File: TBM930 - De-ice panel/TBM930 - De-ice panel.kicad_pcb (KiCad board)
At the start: 2 copper layers, 190.5 x 101.6 mm, 48 parts, among them J1 SW_AIRFRAME_DE_ICE, J2 SW_ICE_LIGHT, J3 SW_PROP_DE_ICE, J4 SW_WIND_SHIELD, J5 SW_PITOT_L_HTR, J6 SW_PITOT_R_HTR, J7 SW_INERT_SEP, J8 Barrel_Jack, SW1 SW_Push, SW2 Mini toggle - SPDT, SW3 Mini toggle - SPDT, SW4 Mini toggle - SPDT, SW5 Mini toggle - SPDT, SW6 Mini toggle - SPDT, SW7 Mini toggle - SPDT, SW8 Mini toggle - SPDT, U1 ArduinoMEGA2560PROEmbed, U2 TLC5917IN, U3 TLC5917IN

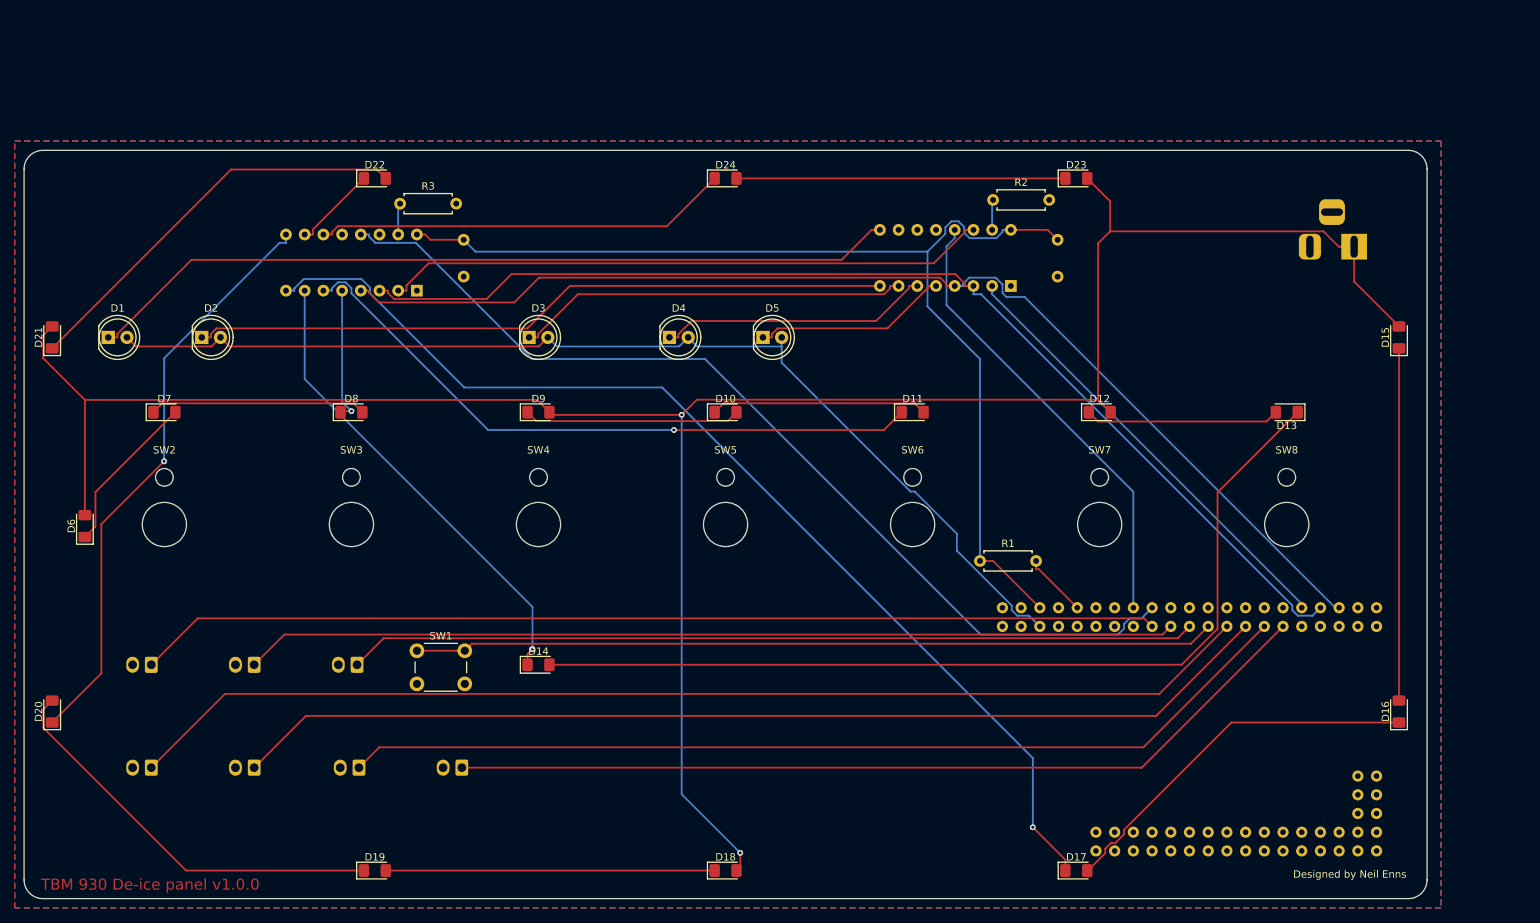
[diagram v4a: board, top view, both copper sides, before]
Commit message: Before switching to Pro Micro
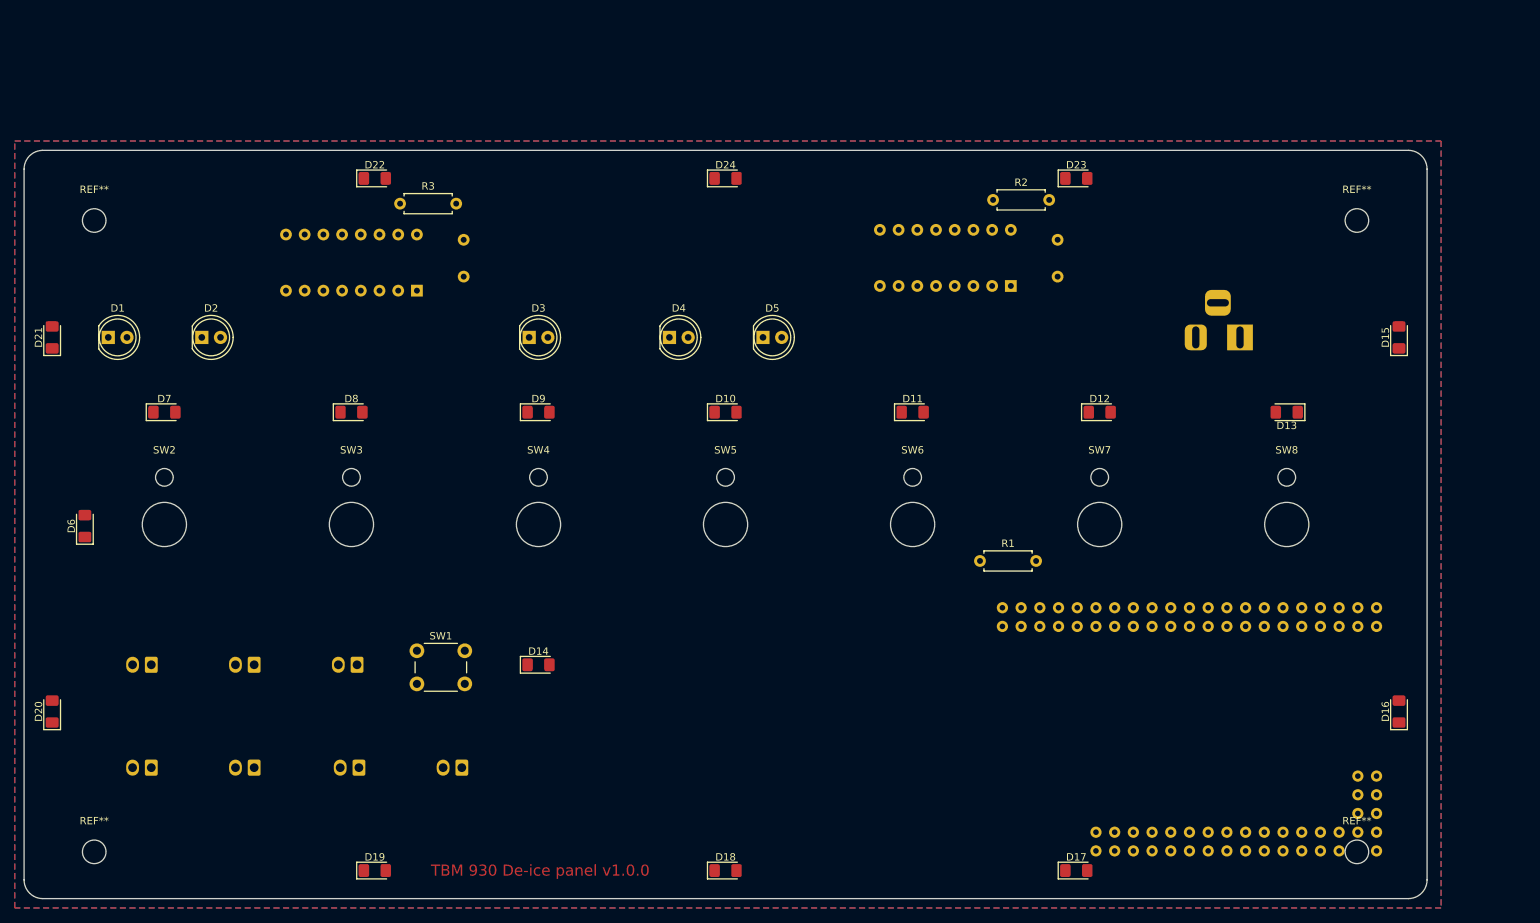
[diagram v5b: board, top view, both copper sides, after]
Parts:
- added REF**: MountingHole_3.2mm_M3, MountingHole:MountingHole_3.2mm_M3, F.Cu at (220.3, 137.8)
- added REF**: MountingHole_3.2mm_M3, MountingHole:MountingHole_3.2mm_M3, F.Cu at (220.3, 52.1)
- added REF**: MountingHole_3.2mm_M3, MountingHole:MountingHole_3.2mm_M3, F.Cu at (48.9, 137.8)
- added REF**: MountingHole_3.2mm_M3, MountingHole:MountingHole_3.2mm_M3, F.Cu at (48.9, 52.1)
- moved J8 19.8 mm to (204.5, 67.9)
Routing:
- net +12V_LED: track 314.9 -> 0.00 mm, vias 2 -> 0
- net LED_LATCH: track 155.6 -> 0.00 mm
- net WIND_SHIELD: track 154.0 -> 0.00 mm
- net LED_CLOCK: track 150.6 -> 0.00 mm
- net +5V: track 148.5 -> 0.00 mm
- net +5V_LED: track 147.5 -> 0.00 mm
- net BACKLIGHT4: track 146.7 -> 0.00 mm, vias 1 -> 0
- net PITOT_L_HTR: track 142.6 -> 0.00 mm
- net AIRFRAME_DE_ICE: track 139.0 -> 0.00 mm
- net BACKLIGHT_BRIGHTNESS: track 132.0 -> 0.00 mm
- net PITOT_R_HTR: track 130.9 -> 0.00 mm
- net Net-(D13-Pad1): track 126.6 -> 0.00 mm
- net ICE_LIGHT: track 126.6 -> 0.00 mm
- net INERT_SEP: track 119.4 -> 0.00 mm
- net PROP_DE_ICE: track 115.2 -> 0.00 mm
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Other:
- board text removed: "Designed by Neil Enns"

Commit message: Switch to smaller Arduino
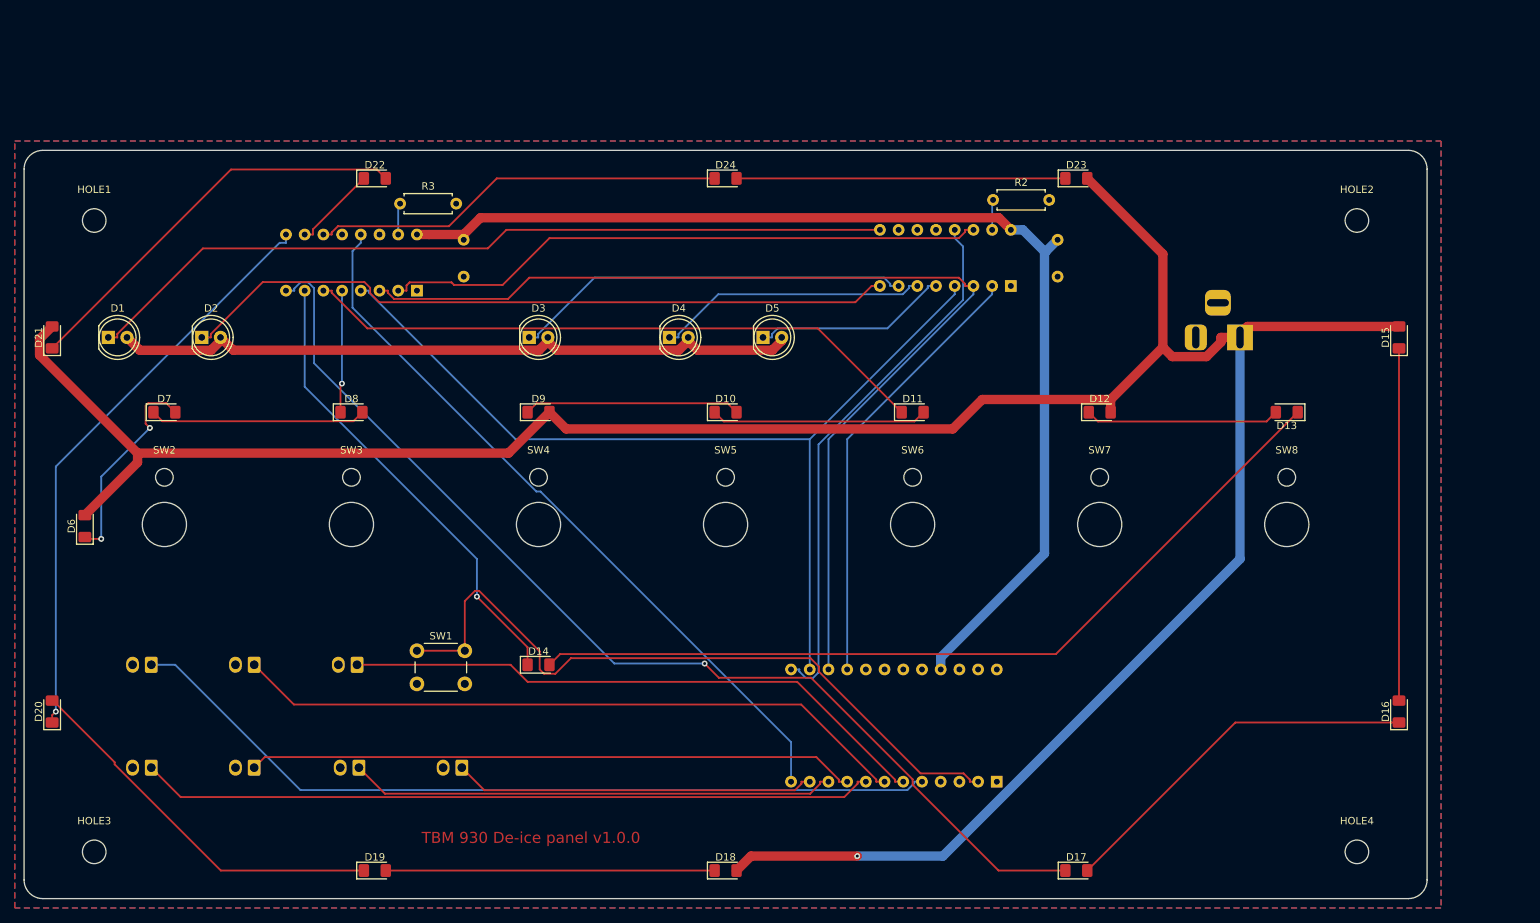
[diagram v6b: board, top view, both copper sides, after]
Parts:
- removed R1: 10k, Resistor_THT:R_Axial_DIN0207_L6.3mm_D2.5mm_P7.62mm_Horizontal
- U1: value ArduinoMEGA2560PROEmbed -> Sparkfun_Pro_Micro; footprint Global MobiFlight panel parts:MEGA2560PROEmbed -> Arduino:Sparkfun_Pro_Micro
- moved U1 54.9 mm to (143.5, 113.0)
- renumbered REF** to HOLE1, REF** to HOLE2, REF** to HOLE3, REF** to HOLE4
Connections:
- U1 pad 10: Net-(U1-Pad10) -> PITOT_R_HTR
- U1 pad 11: Net-(U1-Pad11) -> INERT_SEP
- U1 pad 12: Net-(U1-Pad12) -> BACKLIGHT_BRIGHTNESS
- U1 pad 13: Net-(U1-Pad13) -> ANNUNCIATOR_BRIGHTNESS
- U1 pad 14: Net-(U1-Pad14) -> LED_LATCH
- U1 pad 15: ANNUNCIATOR_BRIGHTNESS -> LED_CLOCK
- U1 pad 16: Net-(U1-Pad16) -> LED_DATA
- U1 pad 17: BACKLIGHT_BRIGHTNESS -> Net-(U1-Pad17)
- U1 pad 18: AIRFRAME_DE_ICE -> Net-(U1-Pad18)
- U1 pad 2: Net-(U1-Pad2) -> LTS_TEST
- U1 pad 20: ICE_LIGHT -> Net-(U1-Pad20)
- U1 pad 21: Net-(U1-Pad21) -> +5V
- U1 pad 22: PROP_DE_ICE -> Net-(U1-Pad22)
- U1 pad 23: Net-(U1-Pad23) -> GND
- U1 pad 24: LTS_TEST -> Net-(U1-Pad24)
- U1 pad 5: +5V -> AIRFRAME_DE_ICE
- U1 pad 6: +5V_LED -> PROP_DE_ICE
- U1 pad 7: Net-(U1-Pad7) -> ICE_LIGHT
- U1 pad 8: Net-(U1-Pad8) -> WIND_SHIELD
- U1 pad 9: Net-(R1-Pad2) -> PITOT_L_HTR
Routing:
- net +12V_LED: track 0.00 -> 361.9 mm, vias 0 -> 1
- net +5V: track 0.00 -> 153.8 mm
- net BACKLIGHT4: track 0.00 -> 145.9 mm, vias 0 -> 1
- net LED_CLOCK: track 0.00 -> 143.3 mm
- net LED_LATCH: track 0.00 -> 129.7 mm
- net Net-(D13-Pad1): track 0.00 -> 115.8 mm
- net AIRFRAME_DE_ICE: track 0.00 -> 112.3 mm
- net AIRFRAME_1: track 0.00 -> 111.1 mm
- net BACKLIGHT_BRIGHTNESS: track 0.00 -> 99.8 mm
- net WIND_SHIELD: track 0.00 -> 99.7 mm
- net LTS_TEST: track 0.00 -> 98.0 mm
- net AIRFRAME_2: track 0.00 -> 97.9 mm
- net +5V_LED: track 0.00 -> 95.2 mm
- net ICE_LIGHT: track 0.00 -> 92.3 mm
- net BACKLIGHT2: track 0.00 -> 85.5 mm
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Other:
- net class +12V_LED added: clearance 0.2, trace_width 1.27, via_dia 0.8, via_drill 0.4
- net class +5V added: clearance 0.2, trace_width 1.27, via_dia 0.8, via_drill 0.4
- net class +5V_LED added: clearance 0.2, trace_width 1.27, via_dia 0.8, via_drill 0.4
- net class GND added: clearance 0.2, trace_width 1.27, via_dia 0.8, via_drill 0.4

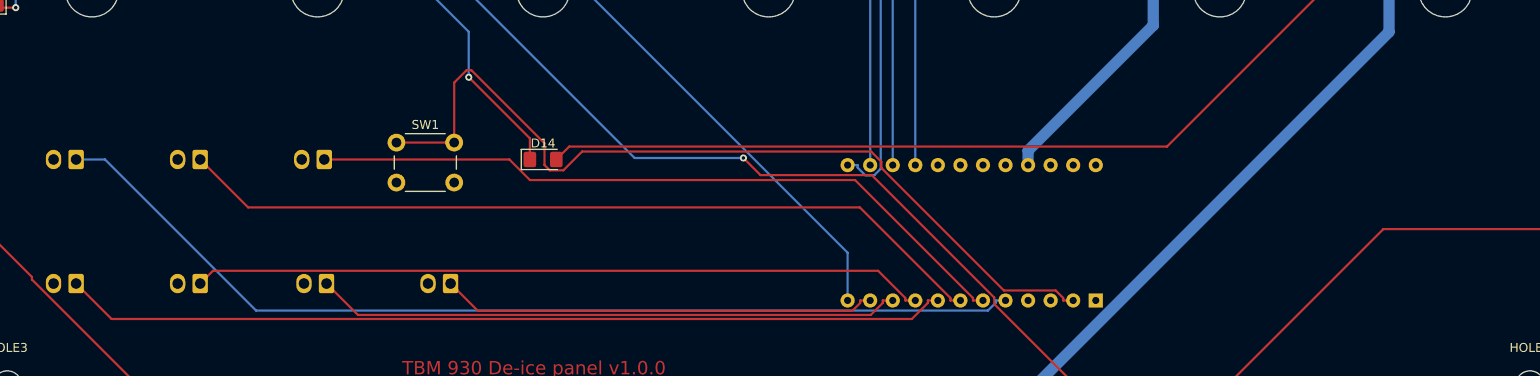
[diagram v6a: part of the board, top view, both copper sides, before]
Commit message: More PCB markings
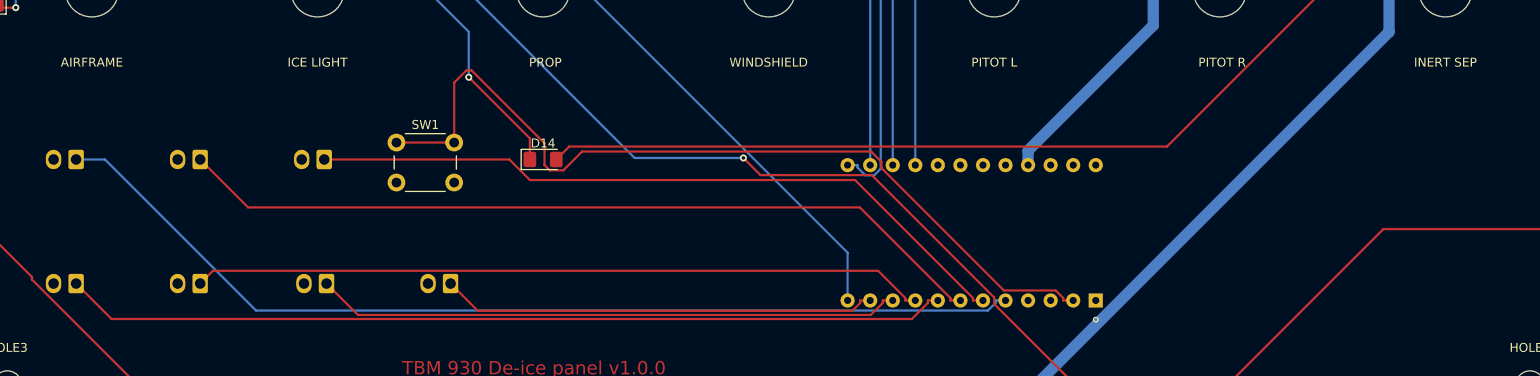
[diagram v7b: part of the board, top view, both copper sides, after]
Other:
- board text added: "+12V"
- board text added: "AIRFRAME"
- board text added: "GND"
- board text added: "ICE LIGHT"
- board text added: "INERT SEP"
- board text added: "PITOT L"
- board text added: "PITOT R"
- board text added: "PROP"
- board text added: "WINDSHIELD"

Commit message: Minor changes
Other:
- board text added: "JLCJLCJLCJLC"
